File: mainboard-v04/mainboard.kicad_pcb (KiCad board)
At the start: 4 copper layers, 90.2 x 95.9 mm, 193 parts, among them J1 503182-1852, J10 Conn_01x05, J11 Conn_01x02, J12 Conn_Coaxial, J13 USB_C_Receptacle_USB2.0, J2 Conn_01x05, J3 Conn_01x01, J4 10118194-0001LF, J5 Conn_Coaxial, J6 Conn_Coaxial, J7 Conn_Coaxial, J8 Conn_01x09, J9 Conn_01x05, Q1 IRLML2803, Q2 2N5088, Q4 IRLML2803, Q5 IRLML2803, SW1 KMR231NG LFS, U1 MAX706RS-T, U10 XTB-40, U11 XTB-40, U12 XTB-40, U13 EP2W+, U14 S1216V8, U15 RFM9xBreakout, U16 PE014006, U17 BQ25883RGER, U18 NDS8434, U19 NDS8434, U2 ATSAMD51J20A-AU, U20 RFM9xBreakout, U23 RFM98PW, U24 RFM98PW, U3 BMX160, U4 ADM1176-1ARMZ-R7, U5 TPS54226PWPRPWP14_2P31X2P46-L, U6 LTC4121, U7 NDS8434, U8 MR25H40MDF, U9 XTB-40, Y1 32.768kHz

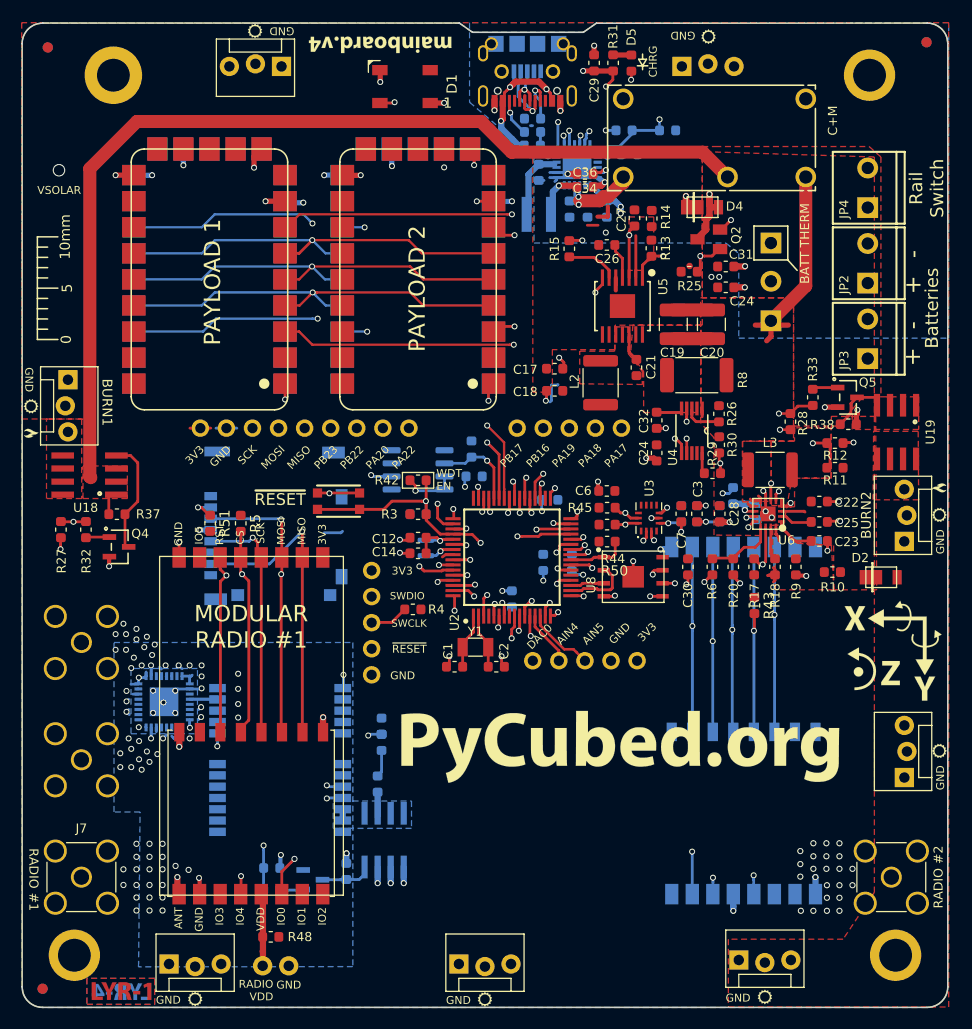
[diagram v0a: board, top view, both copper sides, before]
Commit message: adding mainbaordv04 layout and BOM
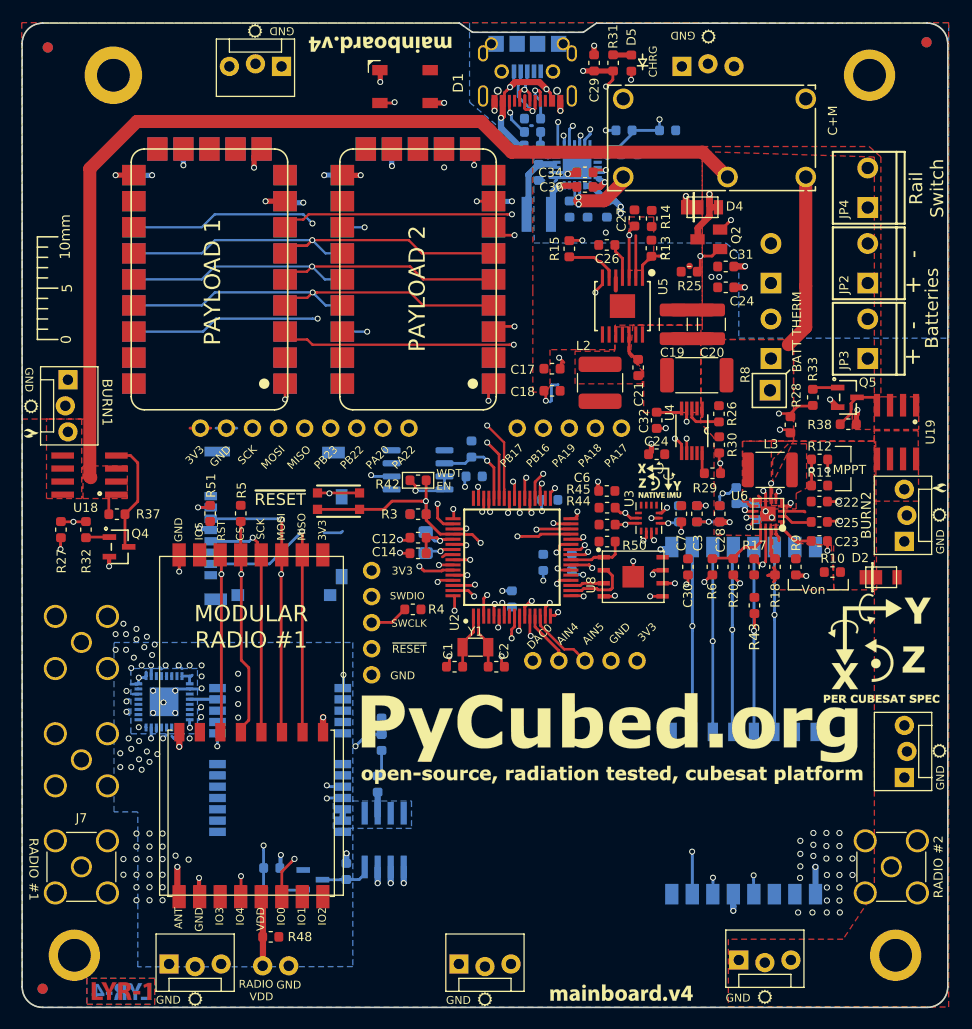
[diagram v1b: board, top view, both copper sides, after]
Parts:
- removed the G*** at (148.6, 125.3)
- removed the REF** at (186.4, 54.4) (x2)
- removed the REF** at (100.8, 54.9) (x2)
- removed the Ref** at (183.1, 113.6)
- added JP1: M023.5MM_LOCK, mainboard:SCREWTERMINAL-3.5MM-2_LOCK, B.Cu at (171.3, 85.0)
- added REF**: Gauge_10mm_Type1_SilkScreenTop, Calibration_Scale:Gauge_10mm_Type1_SilkScreenTop, B.Cu at (99.8, 73.3)
- added REF**: Fiducial_1mm_Mask2mm, Fiducial:Fiducial_1mm_Mask2mm, B.Cu at (186.4, 54.4)
- added REF**: Fiducial_1mm_Mask2mm, Fiducial:Fiducial_1mm_Mask2mm, F.Cu at (186.4, 54.4)
- added REF**: Fiducial_1mm_Mask2mm, Fiducial:Fiducial_1mm_Mask2mm, B.Cu at (100.8, 54.9)
- added REF**: Fiducial_1mm_Mask2mm, Fiducial:Fiducial_1mm_Mask2mm, F.Cu at (100.8, 54.9)
- added Ref**: Val**, custom-footprints:rex-lab, F.Cu at (143.0, 132.6)
- added Ref**: Val**, custom-footprints:XYZ_cubesat-bot, F.Cu at (156.1, 81.4)
- added Ref**: Val**, custom-footprints:XYZ_cubesat-top, F.Cu at (182.0, 113.8)
- added Ref**: Val**, custom-footprints:XYZ_bmx-top, F.Cu at (160.5, 97.2)
- added Ref**: Val**, custom-footprints:mainboard_version, B.Cu at (155.9, 146.9)
- added Ref**: Val**, custom-footprints:opensource, F.Cu at (154.3, 125.1)
- added Ref**: Val**, custom-footprints:mainboard_version, F.Cu at (156.8, 147.2)
- L1: footprint Inductor_SMD:L_0806_2016Metric -> Inductor_SMD:L_0805_2012Metric_Pad1.15x1.40mm_HandSolder
- L2: footprint Inductor_SMD:L_1812_4532Metric -> custom-footprints:L_2141
- L3: value 56uH -> 33uH
- R10: value 40.2K -> 0 or 464K
- R11: value 330K -> 787K
- R12: value 43K -> 121K
- R20: value 6.04K -> 3.01K
- R6: value 10k -> 4.7k
- R9: value 100K -> 107K
- U1: value MAX706RS-T -> MAX706RESA
- moved Ref** 23.7 mm to (132.9, 144.3)
- moved J3 14.4 mm to (171.2, 88.3)
- moved Ref** 5.46 mm to (143.4, 146.8)
- moved Ref** 4.15 mm to (153.0, 121.4)
- moved Ref** 3.81 mm to (170.7, 146.8)
- moved JP5 3.68 mm to (171.3, 77.6)
- moved R11 2.29 mm to (176.0, 97.5)
- moved R12 2.19 mm to (176.0, 95.0)
- moved J12 1.00 mm to (183.0, 134.7)
- moved J7 1.00 mm to (104.1, 134.7)
- moved R5 0.97 mm to (119.6, 100.3)
- moved R51 0.97 mm to (116.6, 100.3)
- moved R28 0.31 mm to (173.2, 91.6)
- moved R19 0.30 mm to (167.9, 98.5)
- moved C17 0.25 mm to (150.0, 86.2)
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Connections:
- C25 pad 2: /Power/VCHRG_IN -> Net-(C25-Pad2)
- JP5 pad 1: VBATT -> Net-(JP1-Pad2)
- L3 pad 2: /Power/VCHRG_IN -> Net-(C25-Pad2)
- U6 pad P$4: /Power/VCHRG_IN -> Net-(C25-Pad2)
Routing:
- net THM: track 24.4 -> 41.2 mm
- net Net-(C25-Pad2): track 0.00 -> 9.68 mm, vias 0 -> 2
- net /Power/VCHRG_IN: track 12.0 -> 2.31 mm, vias 2 -> 0
- net Net-(JP1-Pad2): track 0.00 -> 3.50 mm
- net Net-(R11-Pad1): track 12.4 -> 9.00 mm
- net GND: track 98.5 -> 95.1 mm, vias 150 -> 153
- net RF1_CS: track 42.0 -> 44.0 mm
- net RF1_ANT: track 11.0 -> 12.1 mm
- net /RF and GPS/RF2_ANT: track 9.05 -> 10.1 mm
- net VBATT: track 58.8 -> 58.2 mm
- net VSOLAR: vias 1 -> 0
- added copper zone on F.Cu, net Net-(C25-Pad2)
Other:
- board text added: "MPPT"
- board text added: "Vfloat"
- board text added: "Von"
- board text removed: "1"
- board text removed: "2"
- board text removed: "VSOLAR"
- board text removed: "rexlab.stanford.edu"
- board text removed: "v3"

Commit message: cleaned up v04
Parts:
- removed R47: 0, Resistor_SMD:R_0603_1608Metric
- removed the REF** at (186.4, 54.4) (x2)
- removed the REF** at (100.8, 54.9) (x2)
- removed Ref**: Val**, custom-footprints:XYZ_cubesat-bot
- removed Ref**: Val**, custom-footprints:XYZ_bmx-top
- added C5: 0.1uF, Capacitor_SMD:C_0603_1608Metric, F.Cu at (140.6, 58.4)
- added J14: USB Jumpers, Connector_PinHeader_2.54mm:PinHeader_1x04_P2.54mm_Vertical, B.Cu at (152.1, 70.2)
- added R41: 10k, Resistor_SMD:R_0603_1608Metric, F.Cu at (155.3, 101.3)
- added REF**: Val**, custom-footprints:XYZ_cubesat-bot, F.Cu at (151.5, 127.8)
- added REF**: Fiducial_1mm_Mask2mm, Fiducial:Fiducial_1mm_Mask2mm, B.Cu at (186.4, 54.4)
- added REF**: Fiducial_1mm_Mask2mm, Fiducial:Fiducial_1mm_Mask2mm, F.Cu at (186.4, 54.4)
- added REF**: Fiducial_1mm_Mask2mm, Fiducial:Fiducial_1mm_Mask2mm, B.Cu at (100.8, 54.9)
- added REF**: Fiducial_1mm_Mask2mm, Fiducial:Fiducial_1mm_Mask2mm, F.Cu at (100.8, 54.9)
- C19, C20: value 220UF -> 100uF
- C27: value 1.0uF -> 1uF
- C37, C38, C39: moved to F.Cu
- J12, J5, J6, J7: value Conn_Coaxial -> Amphenol_901-144
- JP1, JP2, JP3, JP4, JP5: value M023.5MM_LOCK -> 1985807
- JP10, JP11, JP12, JP13, JP14, JP15, JP8, JP9: value M03POLAR_LOCK -> Conn_01x03
- L4: footprint custom-footprints:XFL4030472MEB -> custom-footprints:L_4141
- R10: value 0 or 464K -> 0
- R11: value 787K -> 10K
- R46: value 0 -> 10K
- R8: value 0.025 -> 1.0
- REF**: renamed from Ref**; value Val** -> VAL**
- U2: value ATSAMD51J20A-AU -> 120MHZ 512KB Flash 64 TQFP
- moved R46 66.4 mm to (161.2, 60.8), turned to 180 degrees
- moved C37 4.25 mm to (149.2, 70.2), turned to 0 degrees
- moved REF** 3.68 mm to (99.8, 79.6)
- moved REF** 3.68 mm to (99.8, 69.6)
- moved C39 3.54 mm to (152.7, 73.0), turned to 0 degrees
- moved C38 2.72 mm to (149.2, 71.8), turned to 0 degrees
- moved R15 2.02 mm to (152.8, 76.1), turned to 180 degrees
- moved C27 1.95 mm to (156.7, 73.0), turned to 180 degrees
- moved R44 1.65 mm to (155.3, 99.7)
- moved C6 1.65 mm to (155.3, 96.4)
- moved R45 1.64 mm to (155.3, 98.1)
- moved H1 1.26 mm to (106.0, 57.6)
- moved H4 1.26 mm to (179.6, 57.6)
- moved R14 1.09 mm to (160.4, 72.3), turned to 180 degrees
- moved D5 1.06 mm to (158.3, 55.5)
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- renumbered Ref** to REF**
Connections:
- net xSDCS renamed SD_CS
- C37 pad 2: VBATT -> Net-(C37-Pad2)
- C38 pad 2: VBATT -> Net-(C37-Pad2)
- C39 pad 2: VCHRG -> Net-(C39-Pad2)
- C4 pad 2: /Avionics/~RESET -> ~RESET
- R3 pad 2: /Avionics/~RESET -> ~RESET
- R42 pad 1: /Avionics/~RESET -> ~RESET
- R46 pad 1: GND -> GNDREF
- R46 pad 2: Net-(R46-Pad2) -> THM
- SW1 pad A: /Avionics/~RESET -> ~RESET
- SW1 pad A': /Avionics/~RESET -> ~RESET
- U14 pad 8: Net-(R46-Pad2) -> Net-(R24-Pad1)
- U17 pad 13: VCHRG -> Net-(C39-Pad2)
- U17 pad 14: VCHRG -> Net-(C39-Pad2)
- U17 pad 15: VBATT -> Net-(C37-Pad2)
- U17 pad 16: VBATT -> Net-(C37-Pad2)
- U2 pad 52: /Avionics/~RESET -> ~RESET
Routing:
- net ~RESET: track 19.4 -> 38.0 mm, vias 1 -> 2
- net /Avionics/~RESET: track 18.6 -> 0.00 mm, vias 1 -> 0
- net Net-(R46-Pad2): track 17.8 -> 0.00 mm, vias 2 -> 0
- net Net-(R24-Pad1): track 2.63 -> 19.4 mm, vias 0 -> 2
- net VCHRG: track 18.2 -> 11.2 mm, vias 4 -> 2
- net Net-(C37-Pad2): track 0.00 -> 5.64 mm, vias 0 -> 1
- net VBATT: track 58.2 -> 52.9 mm, vias 4 -> 2
- net GND: track 95.1 -> 98.1 mm, vias 153 -> 155
- net Net-(R41-Pad1): track 0.00 -> 2.79 mm
- net GNDREF: track 12.0 -> 14.6 mm, vias 6 -> 9
- net Net-(C35-Pad2): track 6.28 -> 8.46 mm
- net Net-(R15-Pad1): track 5.12 -> 3.06 mm
- net VBUS_IN: track 32.5 -> 30.5 mm
- net SCL: track 63.0 -> 64.5 mm
- net Net-(C39-Pad2): track 0.00 -> 1.51 mm, vias 0 -> 1
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- added copper zone on B.Cu, net Net-(C37-Pad2)
- added copper zone on B.Cu, net Net-(C39-Pad2)
- added copper zone on F.Cu, net VBUS_IN
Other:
- rule via_min_size: 0.5842 -> 0.4318
- board text added: "VCHRG"
- board text added: "VUSB"
